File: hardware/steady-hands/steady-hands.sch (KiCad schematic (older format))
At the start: 25 parts, among them J1 Conn_01x02, Q1 VND5N07-E, U1 BGM13S, U2 BNO055, U4 APDS-9930

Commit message: Edits development board schematic
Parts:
- removed C1: 6.8n, symbol Device:C
- removed C2: CapSense_01x08, Sij_Touch:TouchSlider-8_35x10mm, symbol Sij_Touch:CapSense_01x08
- removed C3: 120n, symbol Device:C
- removed C4, C5: 100n, symbol Device:C
- removed C6: 100u, symbol Device:C
- removed C7, C8, C9: 1u, symbol Device:C
- removed D1: 1N4148WS, Diode_SMD:D_SOD-323, symbol Diode:1N4148WS
- removed J1: Conn_01x02, symbol Connector_Generic:Conn_01x02
- removed Q1: VND5N07-E, Package_TO_SOT_SMD:TO-252-2, symbol Device:Q_NMOS_GDS
- removed R1, R12, R4, R6: 10k, symbol Device:R
- removed R10, R11, R2, R3: 4.7k, symbol Device:R
- removed R5: 0, symbol Device:R
- removed R7: 22, symbol Device:R
- removed U1: BGM13S, Sij_MCU:BGM13S, symbol Sij_MCU:BGM13S
- removed U2: BNO055, Package_LGA:LGA-28_5.2x3.8mm_P0.5mm, symbol Sensor_Motion:BNO055
- removed U4: APDS-9930, QFN_DS-9930, symbol Sij_Sensors:APDS-9930
- added U?: STM32F411CEUx, Package_DFN_QFN:QFN-48-1EP_7x7mm_P0.5mm_EP5.6x5.6mm, symbol MCU_ST_STM32F4:STM32F411CEUx
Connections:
- net labels added: INT2, UART_CTS, UART_RTS, UART_RX, UART_TX, nRESET1
- net labels removed: BL_IND, GND, GNDPWR, I2C_ADDR_SEL, OSC_input, OSC_output, POWER, SCL1, SDA1, SWCLK, SWDIO, V+, V-, VDD, VDDIO, nBOOT_LOAD_PIN
- wire segments 119 -> 28

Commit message: Adds new components
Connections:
- net labels added: EN1
- wire segments 28 -> 30
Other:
- moved on the sheet: U?
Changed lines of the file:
@@
 $Descr A4 11693 8268
 encoding utf-8
-Sheet 1 6
+Sheet 1 7
 Title ""
 Date ""
@@
 Comment4 ""
 $EndDescr
-Text Label 6700 3900 0    50   ~ 0
+Text Label 6550 4050 0    50   ~ 0
 EN
 Wire Wire Line
-	6550 3900 6700 3900
-Text HLabel 9100 1950 2    50   Input ~ 0
-SDA
-Text HLabel 9100 2050 2    50   Input ~ 0
-SCL
-Text HLabel 9100 2150 2    50   Input ~ 0
+	6400 4050 6550 4050
+Text HLabel 9100 1600 2    50   Input ~ 0
+SDA
+Text HLabel 9100 1700 2    50   Input ~ 0
+SCL
+Text HLabel 9100 1800 2    50   Input ~ 0
 INT1
 $Sheet
-S 9000 1900 750  400
+S 9000 1500 750  500
 U 5EF43BAC
 F0 "BNO055" 50
@@
 $EndSheet
 Wire Wire Line
-	9100 1950 8850 1950
-Wire Wire Line
-	9100 2050 8850 2050
-Wire Wire Line
-	9100 2150 8850 2150
-Text Label 8850 1950 2    50   ~ 0
-SDA
-Text Label 8850 2050 2    50   ~ 0
-SCL
-Text Label 8850 2150 2    50   ~ 0
+	9100 1600 8850 1600
+Wire Wire Line
+	9100 1700 8850 1700
+Wire Wire Line
+	9100 1800 8850 1800
+Text Label 8850 1600 2    50   ~ 0
+SDA
+Text Label 8850 1700 2    50   ~ 0
+SCL
+Text Label 8850 1800 2    50   ~ 0
 INT1
 $Sheet
-S 9000 2550 750  400
+S 9000 2200 750  400
 U 5EF838FE
 F0 "APDS-9960" 50
 F1 "APDS-9960.sch" 50
 $EndSheet
-Text HLabel 9100 2650 2    50   Input ~ 0
-SDA
-Text HLabel 9100 2750 2    50   Input ~ 0
-SCL
-Text HLabel 9100 2850 2    50   Input ~ 0
+Text HLabel 9100 2300 2    50   Input ~ 0
+SDA
+Text HLabel 9100 2400 2    50   Input ~ 0
+SCL
+Text HLabel 9100 2500 2    50   Input ~ 0
 INT
 Wire Wire Line
-	9100 2650 8850 2650
-Wire Wire Line
-	9100 2750 8850 2750
-Wire Wire Line
-	9100 2850 8850 2850
-Text Label 8850 2650 2    50   ~ 0
-SDA
-Text Label 8850 2750 2    50   ~ 0
-SCL
-Text Label 8850 2850 2    50   ~ 0
+	9100 2300 8850 2300
+Wire Wire Line
+	9100 2400 8850 2400
+Wire Wire Line
+	9100 2500 8850 2500
+Text Label 8850 2300 2    50   ~ 0
+SDA
+Text Label 8850 2400 2    50   ~ 0
+SCL
+Text Label 8850 2500 2    50   ~ 0
 INT
 $Comp
 L MCU_ST_STM32F4:STM32F411CEUx U?
 U 1 1 5EF9373D
-P 5500 3650
-F 0 "U?" H 5450 5331 50  0000 C CNN
-F 1 "STM32F411CEUx" H 5450 5240 50  0000 C CNN
-F 2 "Package_DFN_QFN:QFN-48-1EP_7x7mm_P0.5mm_EP5.6x5.6mm" H 4900 2150 50  0001 R CNN
-F 3 "http://www.st.com/st-web-ui/static/active/en/resource/technical/document/datasheet/DM00115249.pdf" H 5500 3650 50  0001 C CNN
-	1    5500 3650
+P 5350 3800
+F 0 "U?" H 5300 5481 50  0000 C CNN
+F 1 "STM32F411CEUx" H 5300 5390 50  0000 C CNN
+F 2 "Package_DFN_QFN:QFN-48-1EP_7x7mm_P0.5mm_EP5.6x5.6mm" H 4750 2300 50  0001 R CNN
+F 3 "http://www.st.com/st-web-ui/static/active/en/resource/technical/document/datasheet/DM00115249.pdf" H 5350 3800 50  0001 C CNN
+	1    5350 3800
 	1    0    0    -1
 $EndComp
 $Sheet
-S 9000 3200 750  400
+S 9000 2850 750  400
 U 5EF97273
 F0 "Motors" 50
 F1 "Motors.sch" 50
 $EndSheet
-Text HLabel 9100 3400 2    50   Input ~ 0
+Text HLabel 9100 3000 2    50   Input ~ 0
 EN
 Wire Wire Line
-	8850 3400 9100 3400
-Text Label 8850 3400 2    50   ~ 0
+	8850 3000 9100 3000
+Text Label 8850 3000 2    50   ~ 0
 EN
 Wire Wire Line
-	4800 4250 4600 4250
-Wire Wire Line
-	4800 4350 4600 4350
-Text Label 4600 4250 2    50   ~ 0
-SCL
-Text Label 4600 4350 2    50   ~ 0
-SDA
-Wire Wire Line
-	6300 4550 6100 4550
-Wire Wire Line
-	6100 4650 6300 4650
-Wire Wire Line
-	6100 4450 6300 4450
-Wire Wire Line
-	6100 4750 6300 4750
-Text Label 6300 4450 0    50   ~ 0
+	4650 4400 4450 4400
+Wire Wire Line
+	4650 4500 4450 4500
+Text Label 4450 4400 2    50   ~ 0
+SCL
+Text Label 4450 4500 2    50   ~ 0
+SDA
+Wire Wire Line
+	6150 4700 5950 4700
+Wire Wire Line
+	5950 4800 6150 4800
+Wire Wire Line
+	5950 4600 6150 4600
+Wire Wire Line
+	5950 4900 6150 4900
+Text Label 6150 4600 0    50   ~ 0
 UART_RX
-Text Label 6300 4550 0    50   ~ 0
+Text Label 6150 4700 0    50   ~ 0
 UART_TX
-Text Label 6300 4650 0    50   ~ 0
+Text Label 6150 4800 0    50   ~ 0
 UART_RTS
-Text Label 6300 4750 0    50   ~ 0
+Text Label 6150 4900 0    50   ~ 0
 UART_CTS
 Wire Wire Line
-	4800 4150 4600 4150
-Wire Wire Line
-	4800 4450 4600 4450
-Text Label 4600 4150 2    50   ~ 0
+	4650 4300 4450 4300
+Wire Wire Line
+	4650 4600 4450 4600
+Text Label 4450 4300 2    50   ~ 0
 INT
-Text Label 4600 4450 2    50   ~ 0
+Text Label 4450 4600 2    50   ~ 0
 INT1
 Wire Wire Line
-	6100 4350 6300 4350
-Text Label 6300 4350 0    50   ~ 0
+	5950 4500 6150 4500
+Text Label 6150 4500 0    50   ~ 0
 nRESET
 $Sheet
-S 9000 3850 750  400
+S 9000 3500 750  400
 U 5EFB8965
 F0 "CapTouch" 50
 F1 "CapTouch.sch" 50
 $EndSheet
-Text HLabel 9100 3950 2    50   Input ~ 0
-SDA
-Text HLabel 9100 4050 2    50   Input ~ 0
-SCL
-Text HLabel 9100 4150 2    50   Input ~ 0
+Text HLabel 9100 3600 2    50   Input ~ 0
+SDA
+Text HLabel 9100 3700 2    50   Input ~ 0
+SCL
+Text HLabel 9100 3800 2    50   Input ~ 0
 INT2
 Wire Wire Line
-	9100 3950 8850 3950
-Wire Wire Line
-	9100 4050 8850 4050
-Wire Wire Line
-	9100 4150 8850 4150
-Text Label 8850 3950 2    50   ~ 0
-SDA
-Text Label 8850 4050 2    50   ~ 0
-SCL
-Text Label 8850 4150 2    50   ~ 0
+	9100 3600 8850 3600
+Wire Wire Line
+	9100 3700 8850 3700
+Wire Wire Line
+	9100 3800 8850 3800
+Text Label 8850 3600 2    50   ~ 0
+SDA
+Text Label 8850 3700 2    50   ~ 0
+SCL
+Text Label 8850 3800 2    50   ~ 0
 INT2
-Text HLabel 9100 2250 2    50   Input ~ 0
+Text HLabel 9100 1900 2    50   Input ~ 0
 nRESET1
 Wire Wire Line
-	9100 2250 8850 2250
-Text Label 8850 2250 2    50   ~ 0
+	9100 1900 8850 1900
+Text Label 8850 1900 2    50   ~ 0
 nRESET1
-Text Label 8850 4700 2    50   ~ 0
+Text Label 8850 4350 2    50   ~ 0
 UART_TX
-Text Label 8850 4800 2    50   ~ 0
+Text Label 8850 4450 2    50   ~ 0
 UART_RX
-Text Label 8850 4900 2    50   ~ 0
+Text Label 8850 4550 2    50   ~ 0
 UART_CTS
-Text Label 8850 5000 2    50   ~ 0
+Text Label 8850 4650 2    50   ~ 0
 UART_RTS
-Text Label 8850 4600 2    50   ~ 0
+Text Label 8850 4250 2    50   ~ 0
 nRESET
 $Sheet
-S 9000 4500 750  600
+S 9000 4150 750  600
 U 5EF722F6
 F0 "Bluetooth" 50
 F1 "Bluetooth.sch" 50
 $EndSheet
-Text HLabel 9100 4600 2    50   Input ~ 0
+Text HLabel 9100 4250 2    50   Input ~ 0
 nRESET
-Text HLabel 9100 4700 2    50   Input ~ 0
+Text HLabel 9100 4350 2    50   Input ~ 0
 UART_TX
-Text HLabel 9100 4800 2    50   Input ~ 0
+Text HLabel 9100 4450 2    50   Input ~ 0
 UART_RX
-Text HLabel 9100 4900 2    50   Input ~ 0
+Text HLabel 9100 4550 2    50   Input ~ 0
 UART_CTS
-Text HLabel 9100 5000 2    50   Input ~ 0
+Text HLabel 9100 4650 2    50   Input ~ 0
 UART_RTS
 Wire Wire Line
-	9100 4600 8850 4600
-Wire Wire Line
-	9100 4700 8850 4700
-Wire Wire Line
-	9100 4800 8850 4800
-Wire Wire Line
-	9100 4900 8850 4900
-Wire Wire Line
-	9100 5000 8850 5000
-Wire Wire Line
-	6550 3750 6700 3750
-Text Label 6700 3750 0    50   ~ 0
+	9100 4250 8850 4250
+Wire Wire Line
+	9100 4350 8850 4350
+Wire Wire Line
+	9100 4450 8850 4450
+Wire Wire Line
+	9100 4550 8850 4550
+Wire Wire Line
+	9100 4650 8850 4650
+Wire Wire Line
+	6400 3900 6550 3900
+Text Label 6550 3900 0    50   ~ 0
 nRESET1
 Wire Wire Line
-	6550 4050 6700 4050
-Text Label 6700 4050 0    50   ~ 0
+	6400 4200 6550 4200
+Text Label 6550 4200 0    50   ~ 0
 INT2
+Text HLabel 9100 3100 2    50   Input ~ 0
+EN1
+Text Label 8850 3100 2    50   ~ 0
+EN1
+Wire Wire Line
+	9100 3100 8850 3100
+Wire Wire Line
+	6400 3750 6550 3750
+Text Label 6550 3750 0    50   ~ 0
+EN1
+$Sheet
+S 9000 5000 750  550
+U 5F021BD7
+F0 "PMIC" 50
+F1 "PMIC.sch" 50
+$EndSheet
 $EndSCHEMATC

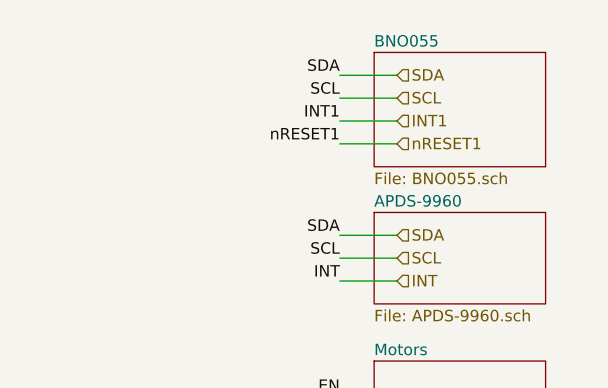
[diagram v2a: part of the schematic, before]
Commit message: Adds symbol library
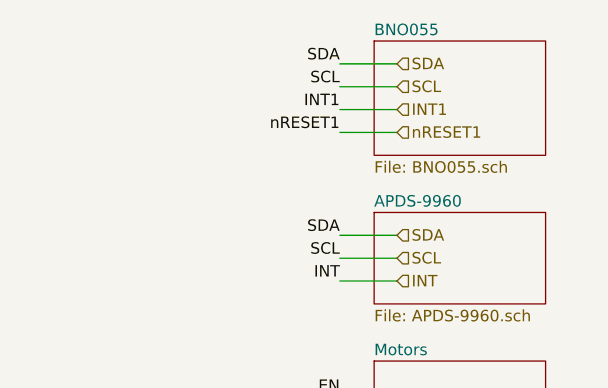
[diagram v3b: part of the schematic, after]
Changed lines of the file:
@@
 Wire Wire Line
 	6400 4050 6550 4050
-Text HLabel 9100 1600 2    50   Input ~ 0
+Text HLabel 9100 1550 2    50   Input ~ 0
 SDA
-Text HLabel 9100 1700 2    50   Input ~ 0
+Text HLabel 9100 1650 2    50   Input ~ 0
 SCL
-Text HLabel 9100 1800 2    50   Input ~ 0
+Text HLabel 9100 1750 2    50   Input ~ 0
 INT1
 $Sheet
-S 9000 1500 750  500
+S 9000 1450 750  500
 U 5EF43BAC
 F0 "BNO055" 50
@@
 $EndSheet
 Wire Wire Line
-	9100 1600 8850 1600
+	9100 1550 8850 1550
 Wire Wire Line
-	9100 1700 8850 1700
+	9100 1650 8850 1650
 Wire Wire Line
-	9100 1800 8850 1800
-Text Label 8850 1600 2    50   ~ 0
+	9100 1750 8850 1750
+Text Label 8850 1550 2    50   ~ 0
 SDA
-Text Label 8850 1700 2    50   ~ 0
+Text Label 8850 1650 2    50   ~ 0
 SCL
-Text Label 8850 1800 2    50   ~ 0
+Text Label 8850 1750 2    50   ~ 0
 INT1
 $Sheet
@@
 Text Label 8850 3800 2    50   ~ 0
 INT2
-Text HLabel 9100 1900 2    50   Input ~ 0
+Text HLabel 9100 1850 2    50   Input ~ 0
 nRESET1
 Wire Wire Line
-	9100 1900 8850 1900
-Text Label 8850 1900 2    50   ~ 0
+	9100 1850 8850 1850
+Text Label 8850 1850 2    50   ~ 0
 nRESET1
 Text Label 8850 4350 2    50   ~ 0

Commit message: Adds power management components
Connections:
- net labels added: +1V3, +3V3, CE, CHG, PGOOD, PWR_EN, PWR_EN1, PWR_EN2
- wire segments 30 -> 39
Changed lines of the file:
@@
 EN1
 $Sheet
-S 9000 5000 750  550
+S 9000 5000 750  900
 U 5F021BD7
-F0 "PMIC" 50
-F1 "PMIC.sch" 50
+F0 "Power Management" 50
+F1 "PwrMgmtsch.sch" 50
 $EndSheet
+Text HLabel 9100 5100 2    50   Input ~ 0
++3V3
+Text HLabel 9100 5200 2    50   Input ~ 0
++1V3
+Text HLabel 9100 5300 2    50   Output ~ 0
+CE
+Text HLabel 9100 5400 2    50   Output ~ 0
+PWR_EN
+Text HLabel 9100 5500 2    50   Output ~ 0
+PWR_EN1
+Text HLabel 9100 5600 2    50   Output ~ 0
+PWR_EN2
+Text HLabel 9100 5700 2    50   Input ~ 0
+PGOOD
+Text HLabel 9100 5800 2    50   Input ~ 0
+CHG
+Wire Wire Line
+	9100 5100 8850 5100
+Wire Wire Line
+	9100 5300 8850 5300
+Wire Wire Line
+	9100 5400 8850 5400
+Wire Wire Line
+	9100 5500 8850 5500
+Wire Wire Line
+	9100 5600 8850 5600
+Wire Wire Line
+	9100 5700 8850 5700
+Wire Wire Line
+	9100 5800 8850 5800
+$Comp
+L power:+3V3 #PWR?
+U 1 1 5F12D7E2
+P 8850 5100
+F 0 "#PWR?" H 8850 4950 50  0001 C CNN
+F 1 "+3V3" H 8865 5273 50  0000 C CNN
+F 2 "" H 8850 5100 50  0001 C CNN
+F 3 "" H 8850 5100 50  0001 C CNN
+	1    8850 5100
+	1    0    0    -1
+$EndComp
+$Comp
+L steady-hands-rescue:+1V3-steady-hands-cache #PWR?
+U 1 1 5F12E82D
+P 8650 5150
+F 0 "#PWR?" H 8650 5350 50  0001 C CNN
+F 1 "+1V3" H 8635 5373 50  0000 C CNN
+F 2 "" H 8650 5350 50  0001 C CNN
+F 3 "" H 8650 5350 50  0001 C CNN
+	1    8650 5150
+	1    0    0    -1
+$EndComp
+Wire Wire Line
+	8650 5200 9100 5200
+Text Label 8850 5300 2    50   ~ 0
+CE
+Text Label 8850 5400 2    50   ~ 0
+PWR_EN
+Text Label 8850 5500 2    50   ~ 0
+PWR_EN1
+Text Label 8850 5600 2    50   ~ 0
+PWR_EN2
+Text Label 8850 5700 2    50   ~ 0
+PGOOD
+Text Label 8850 5800 2    50   ~ 0
+CHG
+Wire Wire Line
+	8650 5100 8650 5200
 $EndSCHEMATC

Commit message: Edits power management components
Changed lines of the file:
@@
 $EndComp
 $Comp
-L steady-hands-rescue:+1V3-steady-hands-cache #PWR?
+L steady-hands:+1V3 #PWR?
 U 1 1 5F12E82D
 P 8650 5150

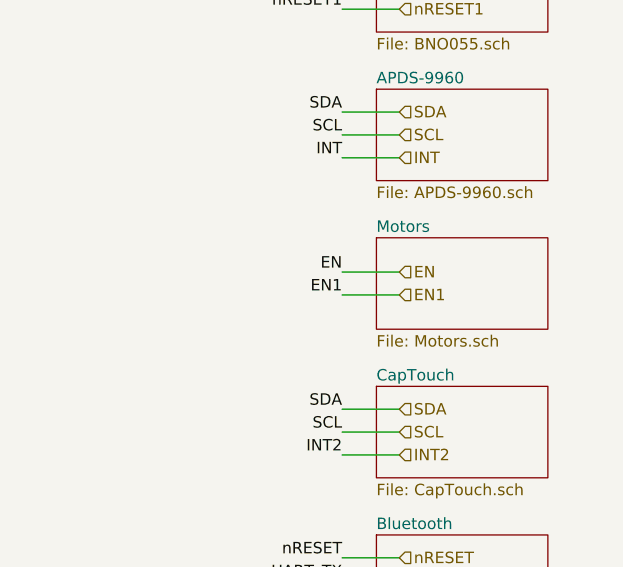
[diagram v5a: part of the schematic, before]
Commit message: Adds second motor components
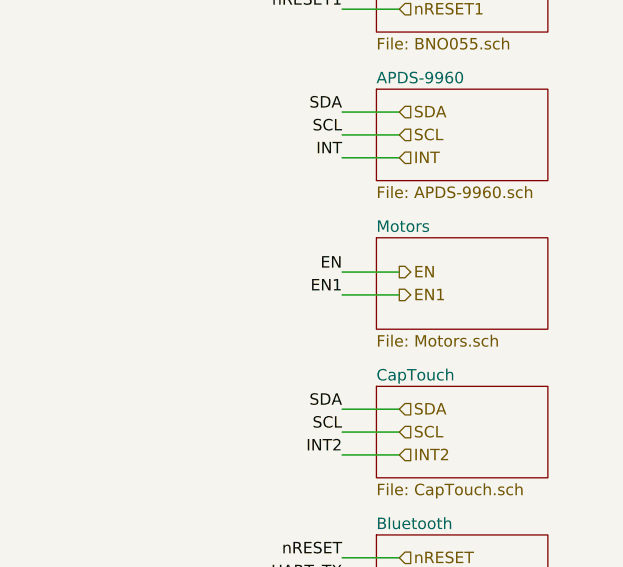
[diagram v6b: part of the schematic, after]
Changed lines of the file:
@@
 F1 "Motors.sch" 50
 $EndSheet
-Text HLabel 9100 3000 2    50   Input ~ 0
+Text HLabel 9100 3000 2    50   Output ~ 0
 EN
 Wire Wire Line
@@
 Text Label 6550 4200 0    50   ~ 0
 INT2
-Text HLabel 9100 3100 2    50   Input ~ 0
+Text HLabel 9100 3100 2    50   Output ~ 0
 EN1
 Text Label 8850 3100 2    50   ~ 0

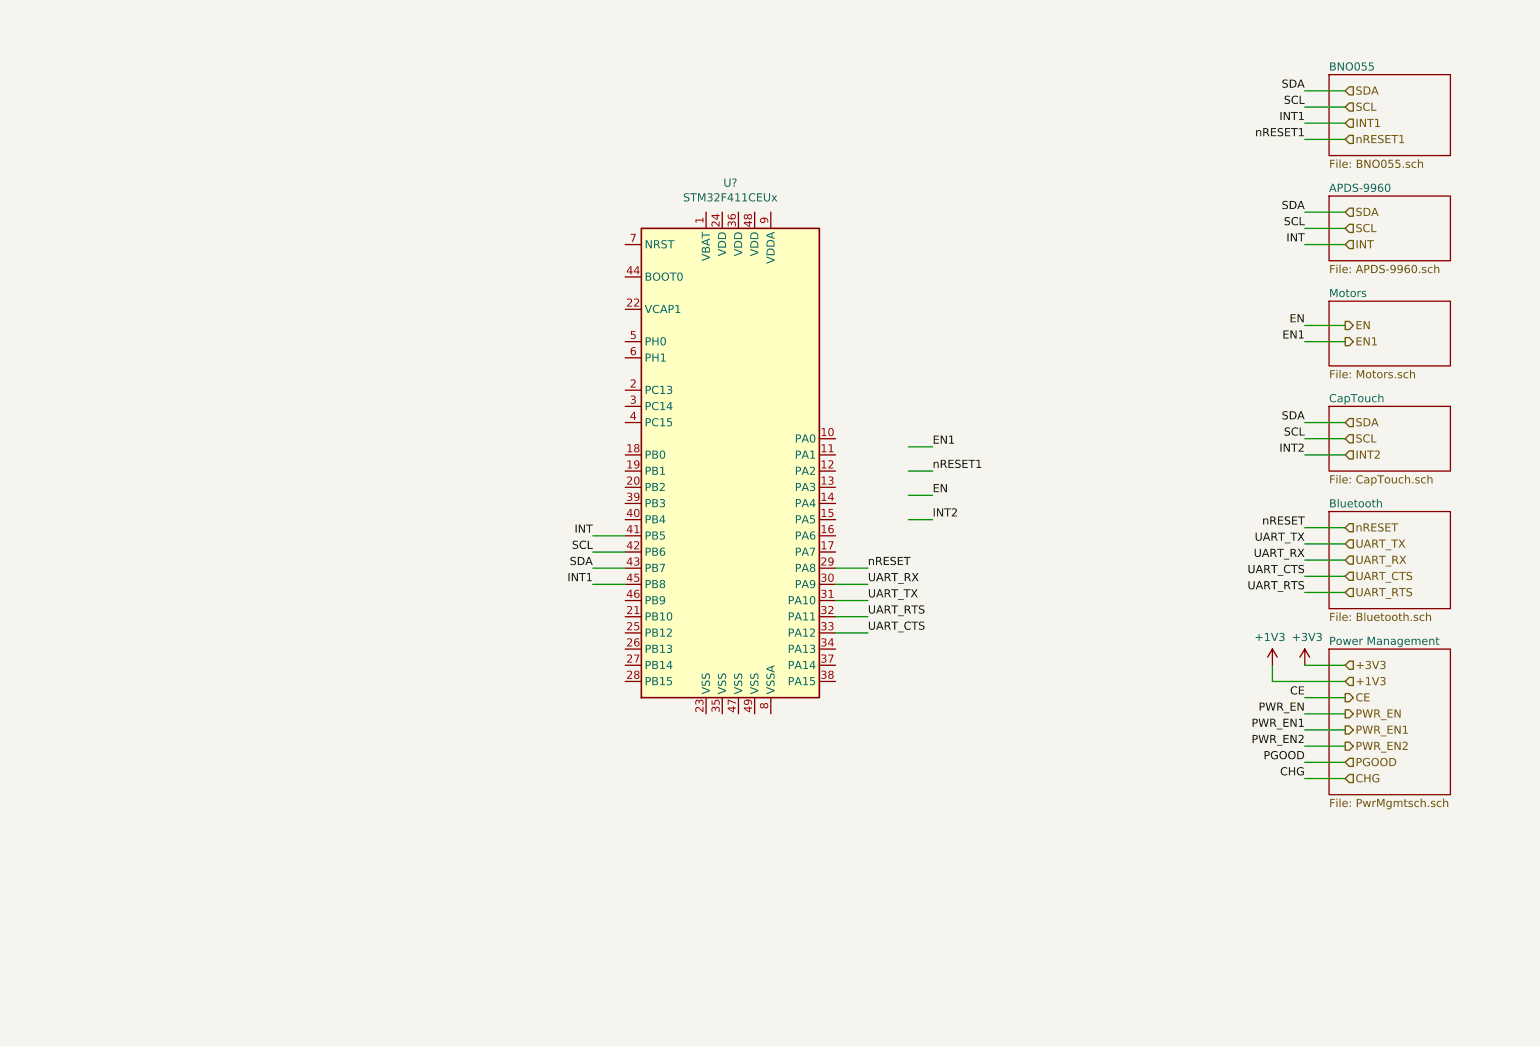
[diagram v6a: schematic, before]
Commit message: Completes schematic connections
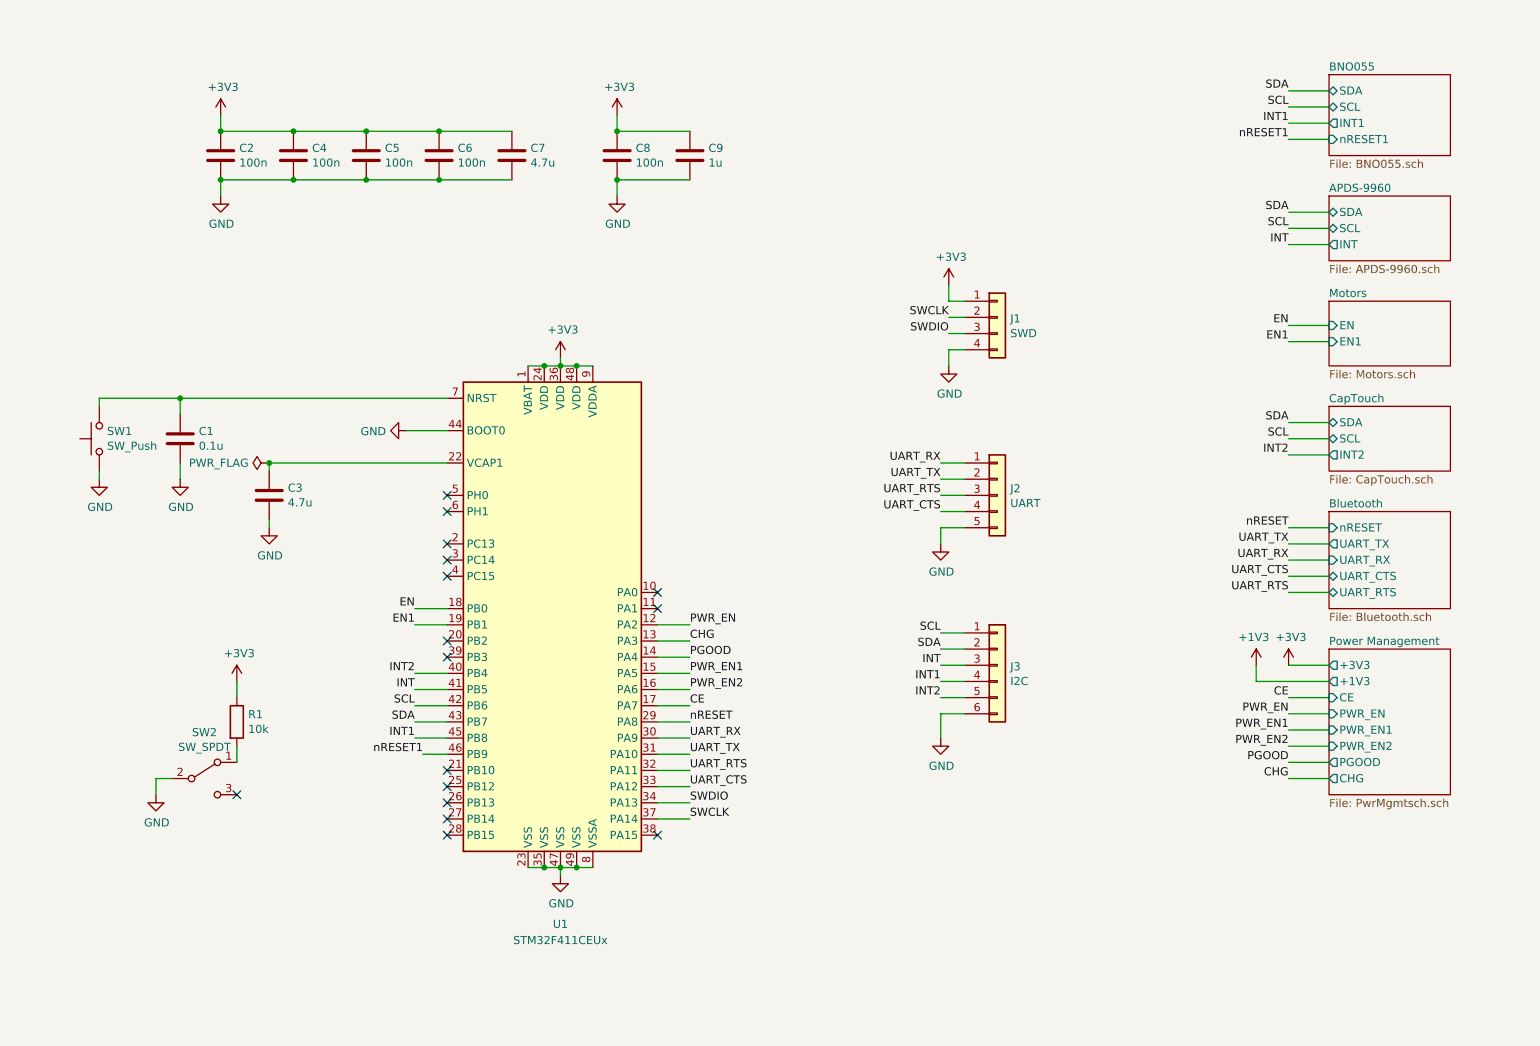
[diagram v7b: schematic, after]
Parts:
- added C1: 0.1u, symbol Device:C
- added C2, C4, C5, C6, C8: 100n, symbol Device:C
- added C3, C7: 4.7u, symbol Device:C
- added C9: 1u, symbol Device:C
- added J1: SWD, symbol Connector_Generic:Conn_01x04
- added J2: UART, symbol Connector_Generic:Conn_01x05
- added J3: I2C, symbol Connector_Generic:Conn_01x06
- added R1: 10k, symbol Device:R
- added SW1: SW_Push, symbol Switch:SW_Push
- added SW2: SW_SPDT, symbol Switch:SW_SPDT
- gave numbers to parts that had none: 1
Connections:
- net labels added: GND, SWCLK, SWDIO
- wire segments 39 -> 104
- no-connect marks 0 -> 16
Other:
- moved on the sheet: U1
